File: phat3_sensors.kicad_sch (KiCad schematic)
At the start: 6 parts, among them U1 MSP430G2553IPW28, U2 BME680

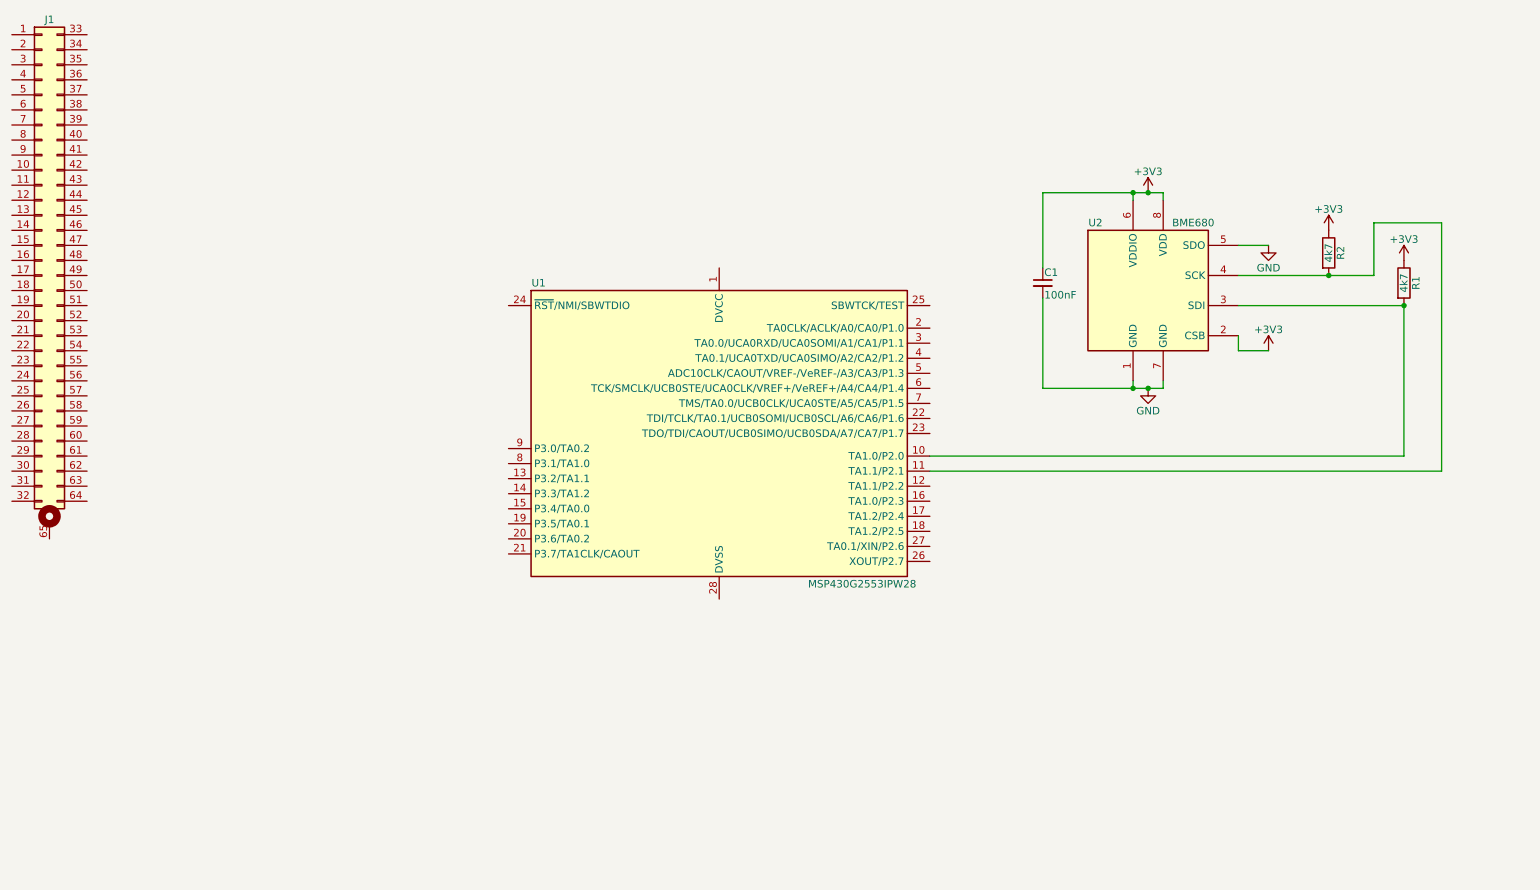
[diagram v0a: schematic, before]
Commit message: Added more sensors
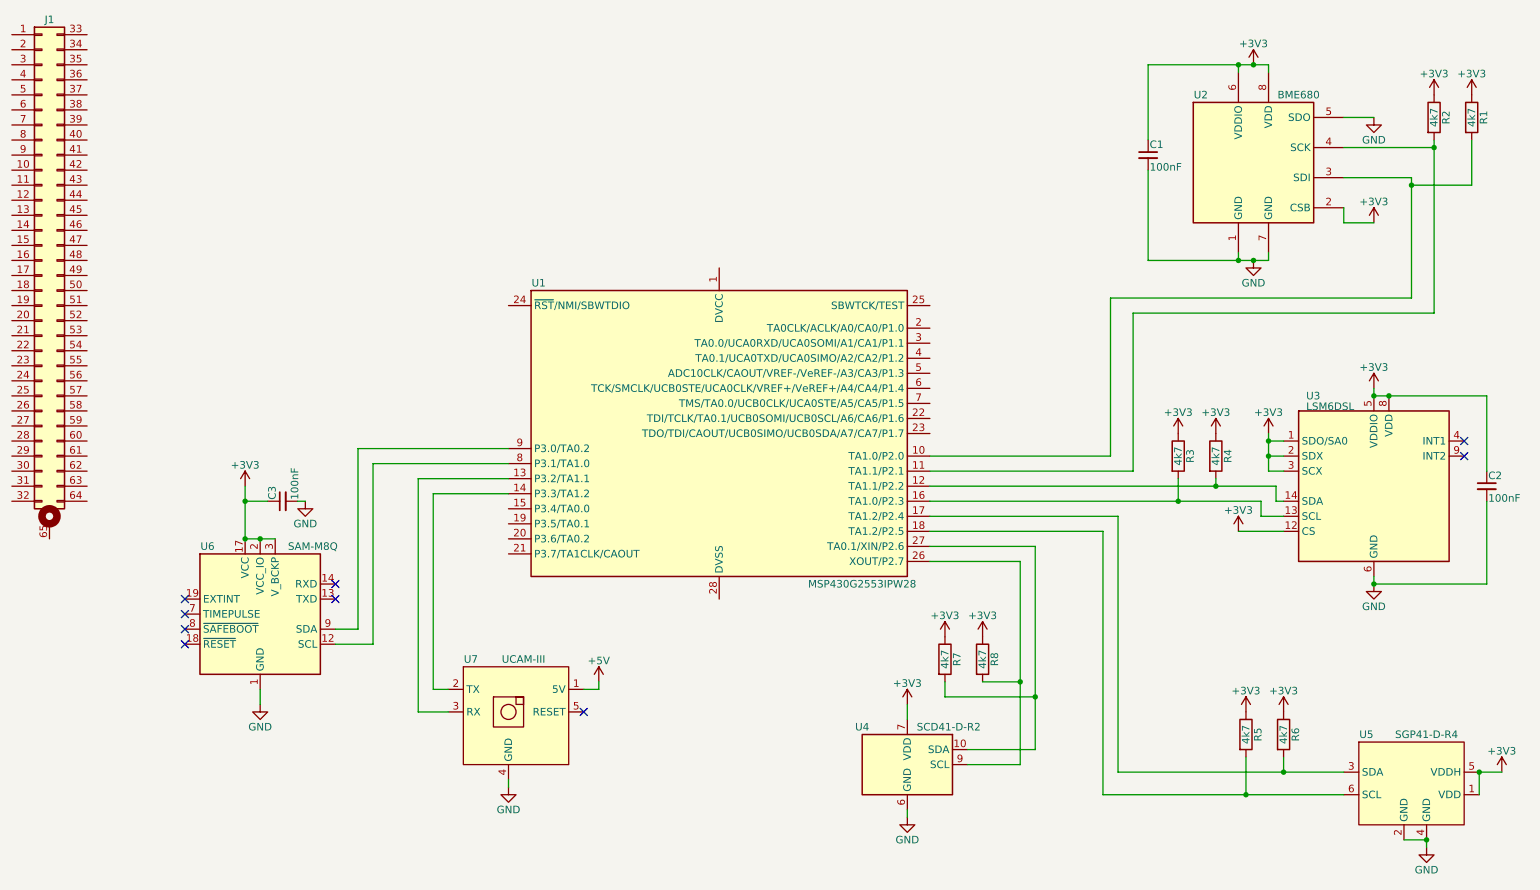
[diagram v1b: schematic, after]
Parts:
- added C2, C3: 100nF, symbol Device:C_Small
- added R3, R4, R5, R6, R7, R8: 4k7, symbol Device:R
- added U3: LSM6DSL, Package_LGA:LGA-14_3x2.5mm_P0.5mm_LayoutBorder3x4y, symbol Sensor_Motion:LSM6DSL
- added U4: SCD41-D-R2, Sensor:Sensirion_SCD4x-1EP_10.1x10.1mm_P1.25mm_EP4.8x4.8mm, symbol Sensor_Gas:SCD41-D-R2
- added U5: SGP41-D-R4, phat3_footprints:DFN_SGP41-D-R4_SEN, symbol HS2_Symbols:SGP41-D-R4
- added U6: SAM-M8Q, RF_GPS:ublox_SAM-M8Q, symbol RF_GPS:SAM-M8Q
- added U7: UCAM-III, symbol HS2_Symbols:UCAM-III
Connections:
- net +3V3: now also C2.1, C3.1, R3.1, R4.1, R5.1, R6.1, R7.1, R8.1, U3.1 (SDO/SA0), U3.12 (CS), U3.2 (SDX), U3.3 (SCX), U3.5 (VDDIO), U3.8 (VDD), U4.19 (VDD), U4.7 (VDD), U5.1 (VDD), U5.5 (VDDH), U6.17 (VCC), U6.2 (VCC_IO), U6.3 (V_BCKP)
- net GND: now also C2.2, C3.2, U3.6 (GND), U3.7 (GND), U4.20 (GND), U4.21 (GND), U4.6 (GND), U5.2 (GND), U5.4 (GND), U6.1 (GND), U6.10 (GND), U6.11 (GND), U6.15 (GND), U6.16 (GND), U6.20 (GND), U6.4 (GND), U6.5 (GND), U6.6 (GND), U7.4 (GND)
- net at U1.12 (TA1.1/P2.2): now also R4.2, U3.14 (SDA)
- net at U1.13 (P3.2/TA1.1): now also U7.3 (RX)
- net at U1.14 (P3.3/TA1.2): now also U7.2 (TX)
- net at U1.16 (TA1.0/P2.3): now also R3.2, U3.13 (SCL)
- net at U1.17 (TA1.2/P2.4): now also R6.2, U5.3 (SDA)
- net at U1.18 (TA1.2/P2.5): now also R5.2, U5.6 (SCL)
- net at U1.26 (XOUT/P2.7): now also R8.2, U4.9 (SCL)
- net at U1.27 (TA0.1/XIN/P2.6): now also R7.2, U4.10 (SDA)
- net at U1.8 (P3.1/TA1.0): now also U6.12 (SCL)
- net at U1.9 (P3.0/TA0.2): now also U6.9 (SDA)
- new net +5V: U7.1 (5V)
- no-connect marks 0 -> 9
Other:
- moved on the sheet: C1, R1, R2, U2
